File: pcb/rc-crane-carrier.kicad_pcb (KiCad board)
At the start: 2 copper layers, 90 x 64 mm, 32 parts, among them J1 BAT 2-3S, J10 SuperMini L, J11 SuperMini R, J12 DIAG0, J13 DIAG1, J2 Motor lift, J3 Motor tele, J4 RC lift, J5 RC tele, U2 TMC2209 #0 lift, U3 TMC2209 #1 tele, U4 LM2940-5.0

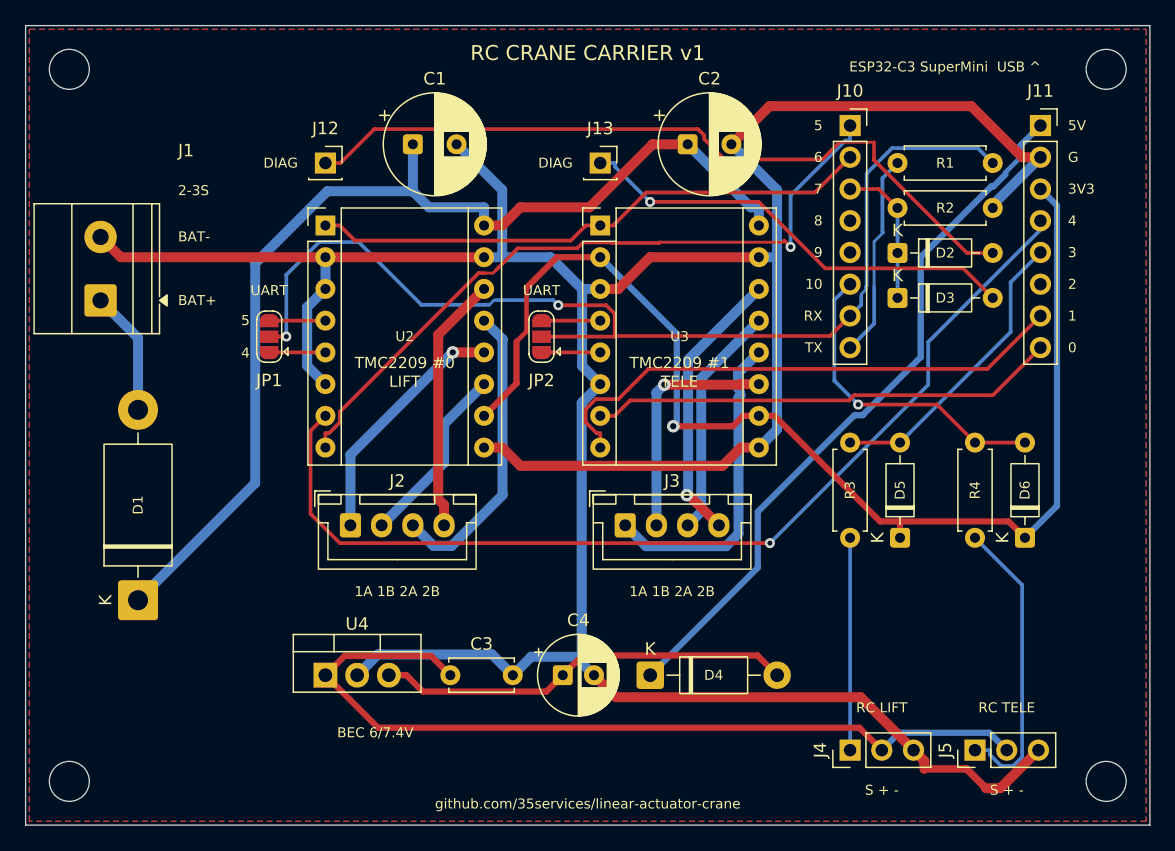
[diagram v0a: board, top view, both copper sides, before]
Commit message: PCB: power the drivers from the BEC, drop the battery input
The drivers' VM now comes from the ESC's BEC (6 V / 7.4 V, 4 A) through
the RC headers, like the ESP32's regulator. Removes the battery
terminal J1 and the reverse polarity diode D1 (the + pin in the middle
of the S + - header makes a reversed servo plug harmless), and the
board shrinks to 80 x 64 mm. Both variants: DRC 0 violations,
0 unconnected.

Co-Authored-By: Claude Opus 5.5 <noreply@anthropic.com>
Claude-Session: https://claude.ai/code/session_01JATcLE25KWRaki615r1Lis
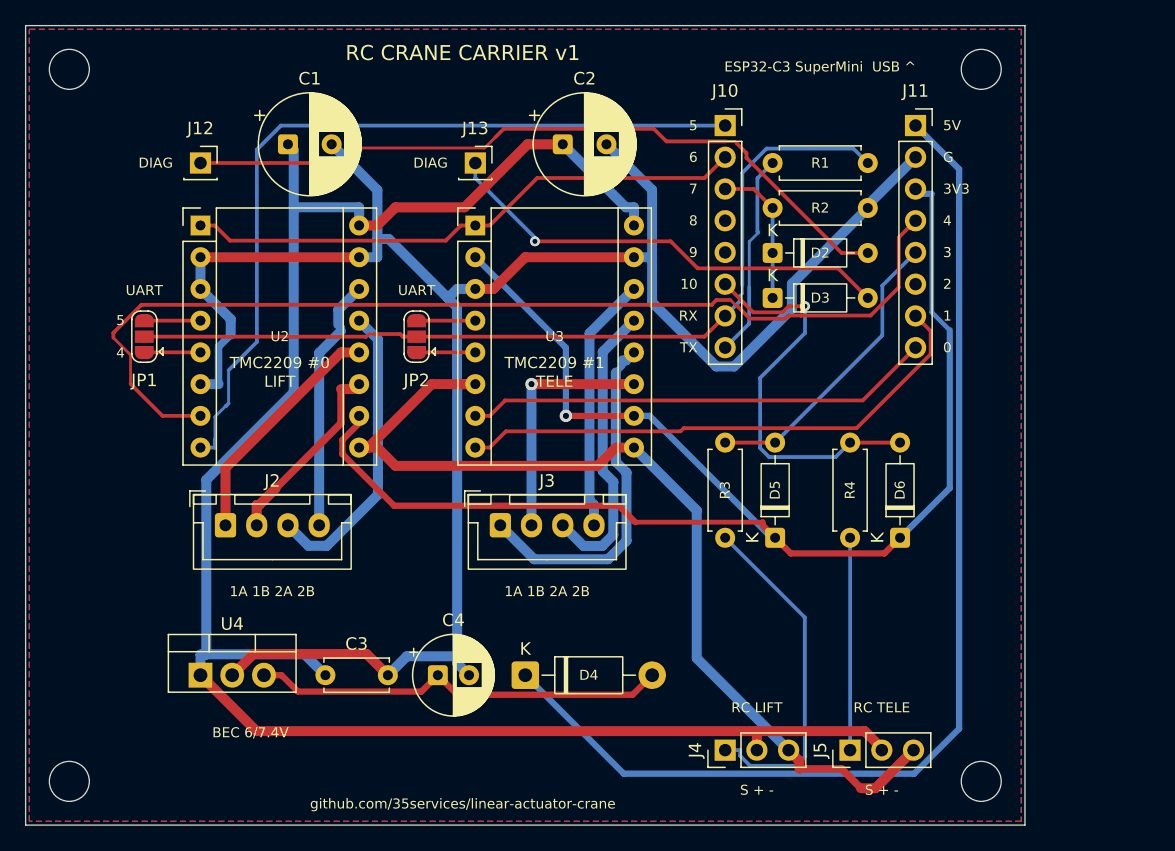
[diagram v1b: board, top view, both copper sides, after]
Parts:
- removed D1: 1N5822, Diode_THT:D_DO-201AD_P15.24mm_Horizontal
- removed J1: BAT 2-3S, TerminalBlock_Phoenix:TerminalBlock_Phoenix_MKDS-1,5-2-5.08_1x02_P5.08mm_Horizontal
- moved C1 10.0 mm to (21.0, 9.50)
- moved C2 10.0 mm to (43.0, 9.50)
- moved C3 10.0 mm to (24.0, 52.0)
- moved C4 10.0 mm to (33.0, 52.0)
- moved D2 10.0 mm to (59.8, 18.2)
- moved D3 10.0 mm to (59.8, 21.8)
- moved D4 10.0 mm to (40.0, 52.0)
- moved D5 10.0 mm to (60.0, 41.0)
- moved D6 10.0 mm to (70.0, 41.0)
- moved H2 10.0 mm to (76.5, 3.50)
- moved H4 10.0 mm to (76.5, 60.5)
- moved J10 10.0 mm to (56.0, 8.00)
- moved J11 10.0 mm to (71.2, 8.00)
- moved J12 10.0 mm to (14.0, 11.0)
- moved J13 10.0 mm to (36.0, 11.0)
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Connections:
- C1 pad 1: VM -> VBEC
- C2 pad 1: VM -> VBEC
- U2 pad 16: VM -> VBEC
- U3 pad 16: VM -> VBEC
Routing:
- net VM: track 85.5 -> 0.00 mm
- net VBEC: track 69.5 -> 149.8 mm
- net +5V: track 57.4 -> 89.2 mm
- net +3V3: track 98.1 -> 119.9 mm
- net GND: track 255.3 -> 237.2 mm
- net UART: track 86.9 -> 70.8 mm, vias 2 -> 0
- net RC0_IN: track 17.0 -> 27.6 mm
- net VBAT_IN: track 10.0 -> 0.00 mm
- net DIR0: track 57.4 -> 64.7 mm, vias 1 -> 0
- net RC1_IN: track 23.9 -> 17.0 mm
- net RC1: track 25.6 -> 32.4 mm
- net M1_2A: track 18.7 -> 23.6 mm
- net M1_1A: track 25.6 -> 28.0 mm
- net STEP0: track 80.9 -> 82.8 mm, vias 1 -> 0
- net M1_2B: track 22.5 -> 20.5 mm, vias 1 -> 0
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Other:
- board size 90 x 64 mm -> 80 x 64 mm
- board text removed: "2-3S"
- board text removed: "BAT+"
- board text removed: "BAT-"
